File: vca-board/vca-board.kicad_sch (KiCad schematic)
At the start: 6 parts, among them U3 TL074

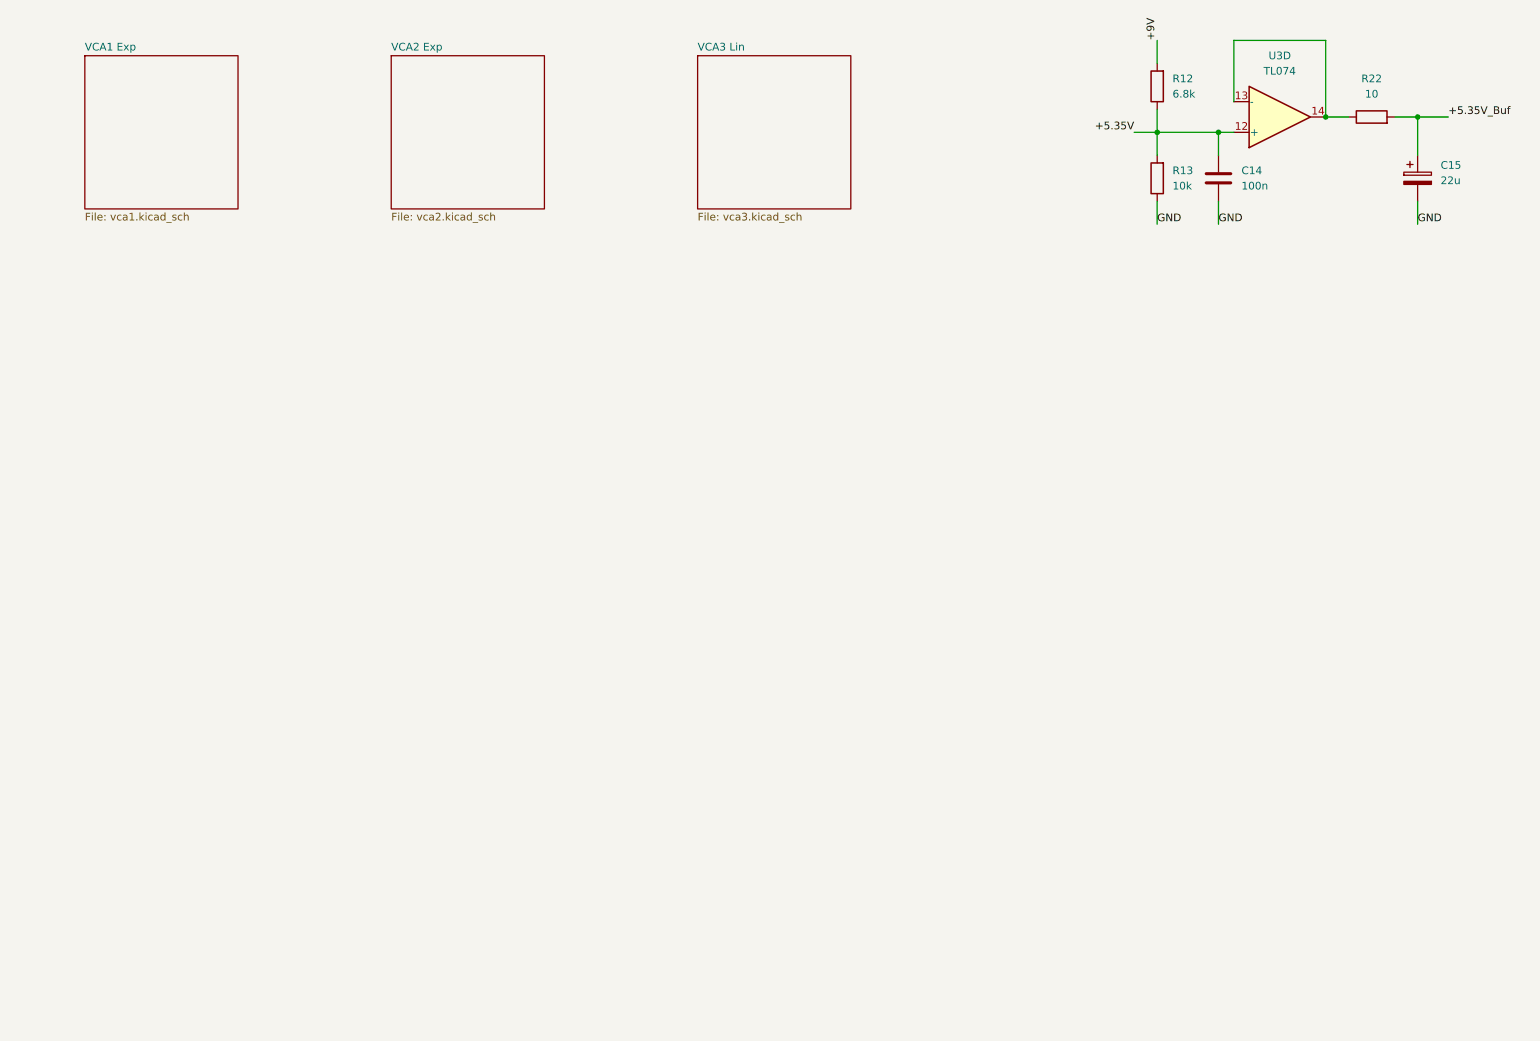
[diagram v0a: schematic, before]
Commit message: VCA components linked
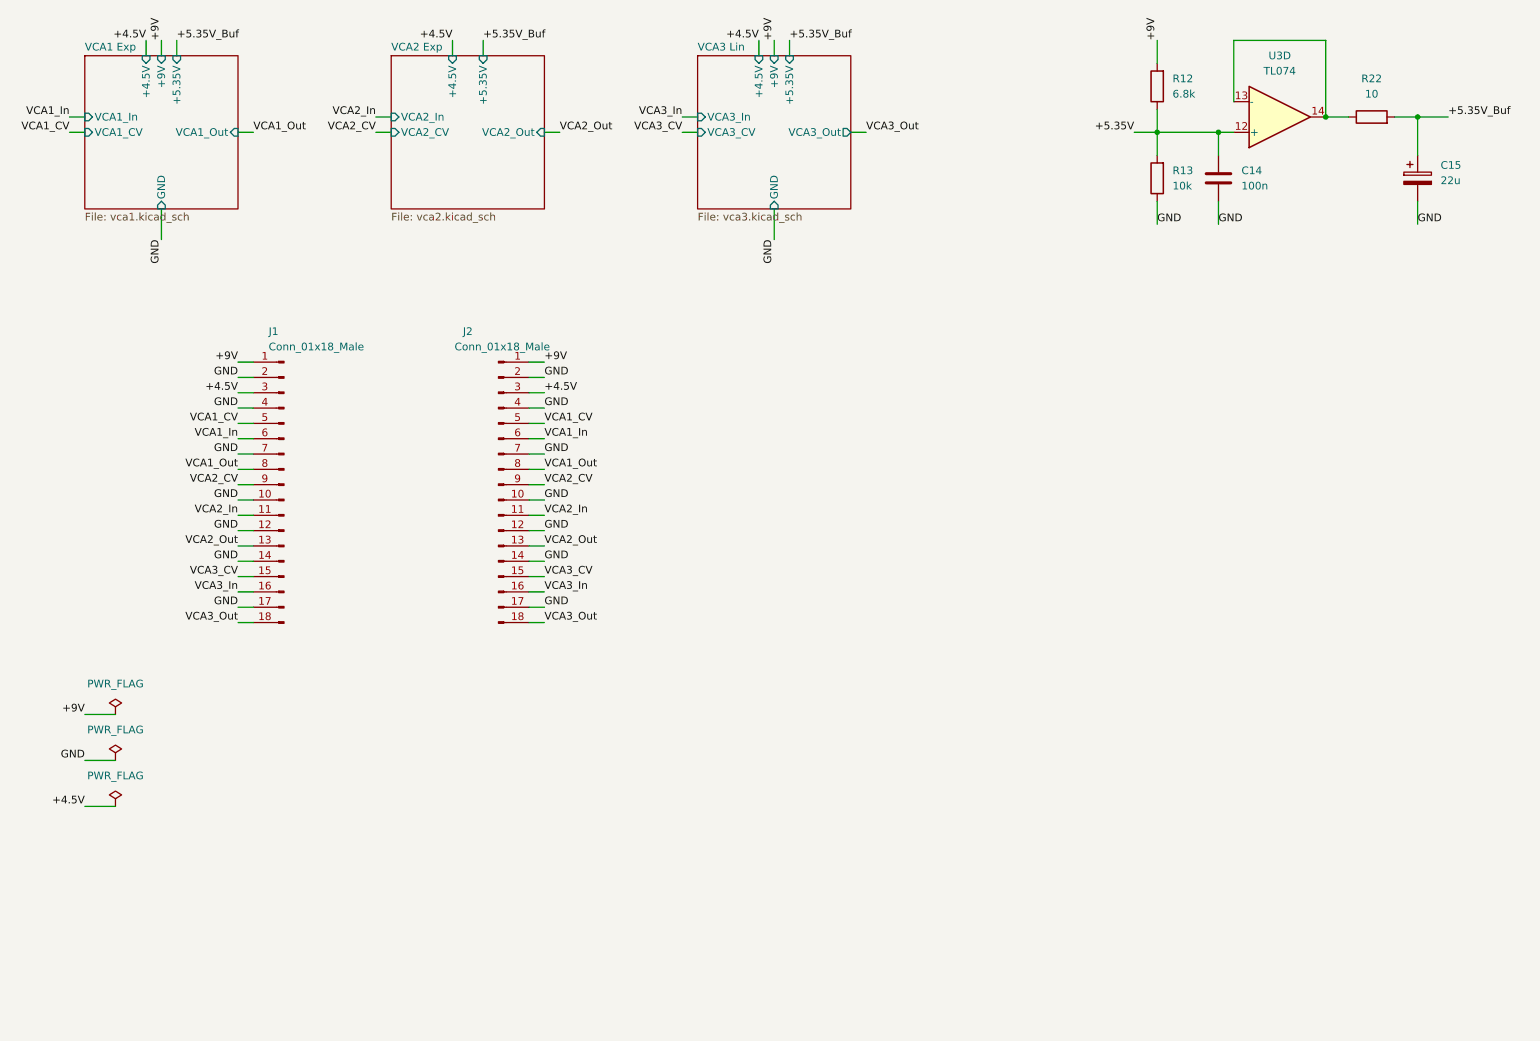
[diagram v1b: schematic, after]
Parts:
- added J1, J2: Conn_01x18_Male, symbol Connector:Conn_01x18_Male
- C14: footprint (none) -> Capacitor_SMD:C_0603_1608Metric_Pad1.08x0.95mm_HandSolder; LCSC (none) -> C76711
- C15: footprint (none) -> Capacitor_Tantalum_SMD:CP_EIA-3216-18_Kemet-A_Pad1.58x1.35mm_HandSolder; LCSC (none) -> C129272
- R12: LCSC (none) -> C23212
- R13: LCSC (none) -> C25804
- R22: LCSC (none) -> C22859
- U3: footprint (none) -> Package_SO:SOIC-14_3.9x8.7mm_P1.27mm; LCSC (none) -> C6963
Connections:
- net +9V: now also J1.1 (Pin_1), J2.1 (Pin_1)
- net GND: now also J1.10 (Pin_10), J1.12 (Pin_12), J1.14 (Pin_14), J1.17 (Pin_17), J1.2 (Pin_2), J1.4 (Pin_4), J1.7 (Pin_7), J2.10 (Pin_10), J2.12 (Pin_12), J2.14 (Pin_14), J2.17 (Pin_17), J2.2 (Pin_2), J2.4 (Pin_4), J2.7 (Pin_7)
- new net +4.5V: J1.3 (Pin_3), J2.3 (Pin_3)
- new net VCA1_CV: J1.5 (Pin_5), J2.5 (Pin_5)
- new net VCA1_In: J1.6 (Pin_6), J2.6 (Pin_6)
- new net VCA1_Out: J1.8 (Pin_8), J2.8 (Pin_8)
- new net VCA2_CV: J1.9 (Pin_9), J2.9 (Pin_9)
- new net VCA2_In: J1.11 (Pin_11), J2.11 (Pin_11)
- new net VCA2_Out: J1.13 (Pin_13), J2.13 (Pin_13)
- new net VCA3_CV: J1.15 (Pin_15), J2.15 (Pin_15)
- new net VCA3_In: J1.16 (Pin_16), J2.16 (Pin_16)
- new net VCA3_Out: J1.18 (Pin_18), J2.18 (Pin_18)
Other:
- sheet VCA1 Exp ports: added +4.5V, +5.35V, +9V, GND, VCA1_CV, VCA1_In, VCA1_Out; removed none
- sheet VCA2 Exp ports: added +4.5V, +5.35V, VCA2_CV, VCA2_In, VCA2_Out; removed none
- sheet VCA3 Lin ports: added +4.5V, +5.35V, +9V, GND, VCA3_CV, VCA3_In, VCA3_Out; removed none

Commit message: VCA board components placed
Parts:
- added H1, H3: GND, MountingHole:MountingHole_3.2mm_M3_ISO14580_Pad, symbol Mechanical:MountingHole_Pad
- added H2: 1, MountingHole:MountingHole_3.2mm_M3, symbol Mechanical:MountingHole
- added H4: 2, MountingHole:MountingHole_3.2mm_M3, symbol Mechanical:MountingHole
- J1, J2: footprint (none) -> Connector_PinHeader_2.54mm:PinHeader_1x18_P2.54mm_Vertical
- R12, R13, R22: footprint (none) -> Resistor_SMD:R_0603_1608Metric_Pad0.98x0.95mm_HandSolder
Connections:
- net GND: now also H1.1, H3.1
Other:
- sheet VCA2 Exp ports: added +9V, GND; removed none

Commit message: wip
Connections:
- net GND: now also J1.9 (Pin_9), J2.9 (Pin_9); no longer J1.10 (Pin_10), J2.10 (Pin_10)
- net VCA2_CV: now also J1.10 (Pin_10), J2.10 (Pin_10); no longer J1.9 (Pin_9), J2.9 (Pin_9)
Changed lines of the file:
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@@
     (effects (font (size 1.27 1.27)) (justify right bottom))
   )
-  (label "GND" (at 101.6 99.06 0)
+  (label "GND" (at 101.6 96.52 0)
     (effects (font (size 1.27 1.27)) (justify left bottom))
   )
@@
     (effects (font (size 1.27 1.27)) (justify right bottom))
   )
-  (label "VCA2_CV" (at 101.6 96.52 0)
+  (label "VCA2_CV" (at 101.6 99.06 0)
     (effects (font (size 1.27 1.27)) (justify left bottom))
   )
@@
     (effects (font (size 1.27 1.27)) (justify left bottom))
   )
-  (label "VCA2_CV" (at 50.8 96.52 180)
+  (label "VCA2_CV" (at 50.8 99.06 180)
     (effects (font (size 1.27 1.27)) (justify right bottom))
   )
@@
     (effects (font (size 1.27 1.27)) (justify left bottom))
   )
-  (label "GND" (at 50.8 99.06 180)
+  (label "GND" (at 50.8 96.52 180)
     (effects (font (size 1.27 1.27)) (justify right bottom))
   )

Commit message: Remove D from linear VCA + update graphics
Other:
- company: (none) -> Pedal Markt / Andrey Salomatin
- title: (none) -> VCA Board
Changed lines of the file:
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@@
 (kicad_sch (version 20211123) (generator eeschema)
   (paper "A4")
+  (title_block
+    (title "VCA Board")
+    (date "2024-11-07")
+    (rev "v1rev2")
+    (company "Pedal Markt / Andrey Salomatin")
+  )
   (junction (at 213.36 38.1) (diameter 0) (color 0 0 0 0)
   )
@@
       (reference "D1") (unit 1) (value "2.7V") (footprint "Diode_SMD:D_SOD-123")
     )
-    (path "/1125607f-c780-4305-b94b-4e1656bf326d/6c3fdc79-8e91-4f59-87fd-39c42d575c1a/8ab18df0-39cd-4004-a0ca-bc629d152af1"
-      (reference "D2") (unit 1) (value "1N4148") (footprint "Diode_SMD:D_SOD-123")
-    )
     (path "/8ba9cbcc-be31-43d8-a61d-149bdca7ca2b/416b7702-1184-4eff-ae17-7880af6dda0d/740fa76a-728c-446f-abec-67b949df6f7c"

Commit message: wip pre-redo orientation
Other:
- company: Pedal Markt / Andrey Salomatin -> Andrey Salomatin / Pedal Markt
- title: VCA Board -> Mag
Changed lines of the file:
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@@
   (paper "A4")
   (title_block
-    (title "VCA Board")
+    (title "Mag")
     (date "2024-11-07")
     (rev "v1rev2")
-    (company "Pedal Markt / Andrey Salomatin")
+    (company "Andrey Salomatin / Pedal Markt")
   )
   (junction (at 213.36 38.1) (diameter 0) (color 0 0 0 0)
